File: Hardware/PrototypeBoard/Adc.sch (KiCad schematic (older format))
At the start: 30 parts, among them U5 ADC124S021

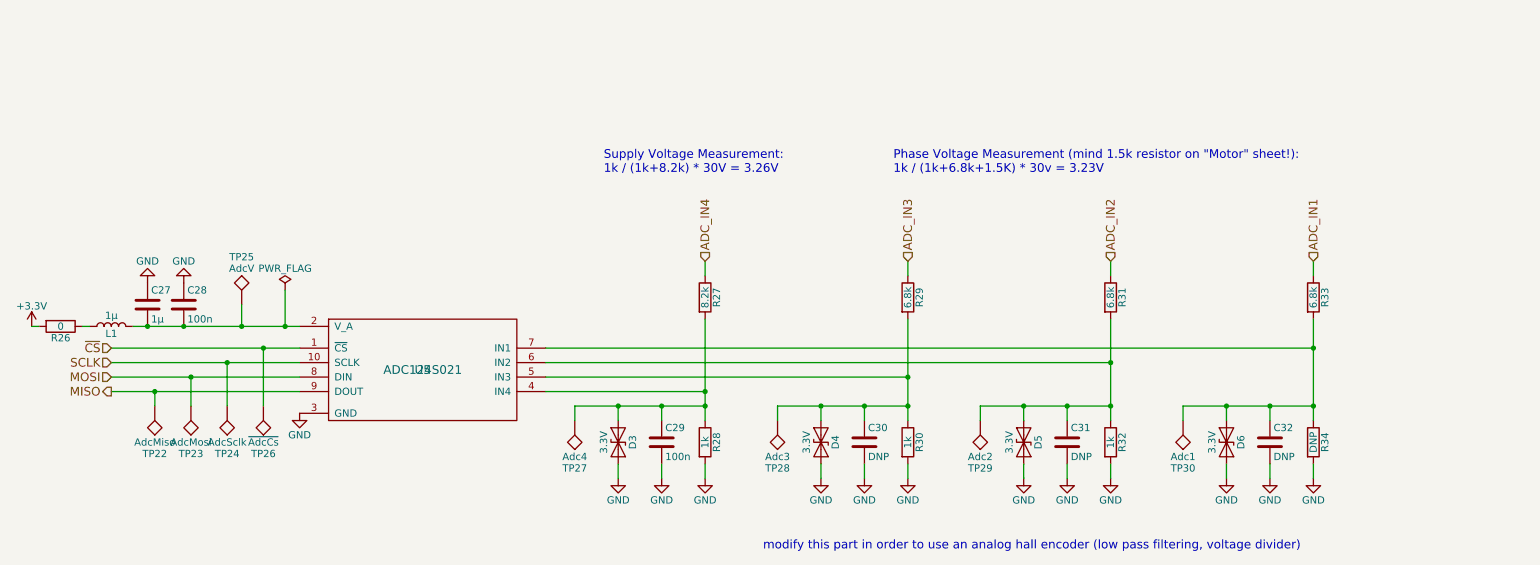
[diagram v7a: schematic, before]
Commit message: Added LEDs for PWM, SPI communication, Gate Driver Errors and Gate Driver disabled
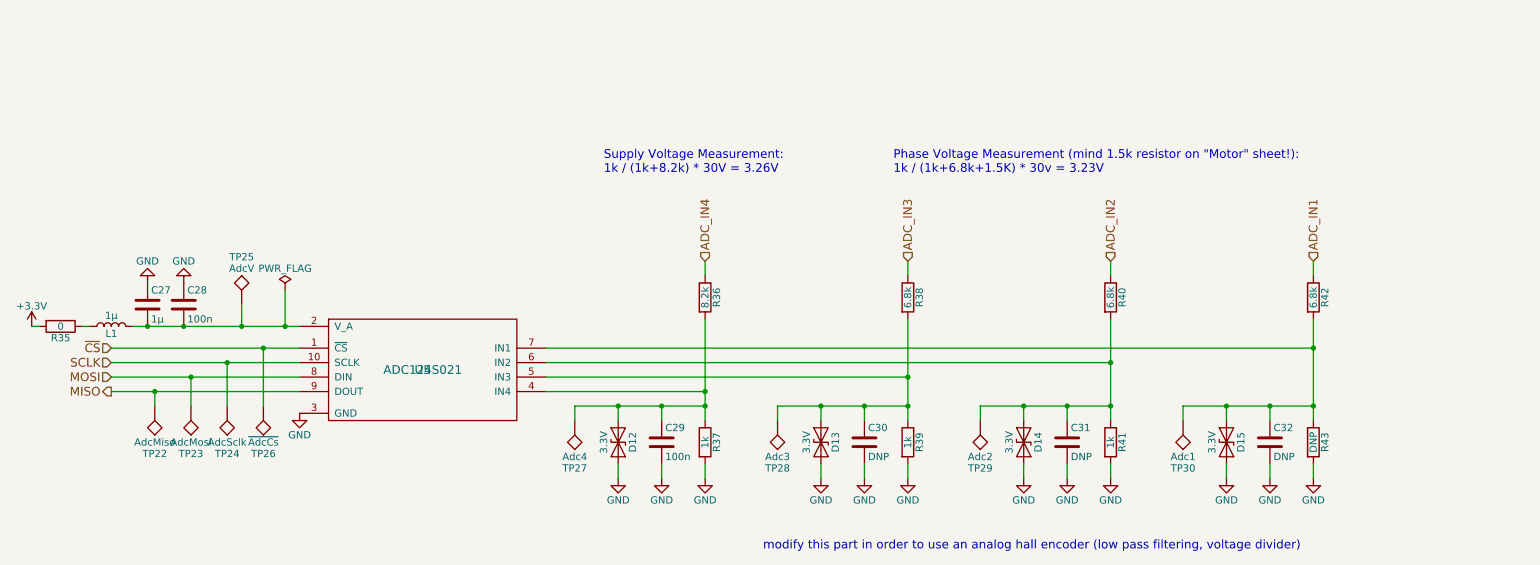
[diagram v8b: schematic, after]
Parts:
- renumbered D3 to D12, D4 to D13, D5 to D14, D6 to D15, R26 to R35, R27 to R36, R28 to R37, R29 to R38, R30 to R39, R31 to R40, R32 to R41, R33 to R42, R34 to R43
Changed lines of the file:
@@
 $EndComp
 $Comp
-L power:GND #PWR0104
+L power:GND #PWR058
 U 1 1 5AFC7F46
 P 2400 2950
-F 0 "#PWR0104" H 2400 2700 50  0001 C CNN
+F 0 "#PWR058" H 2400 2700 50  0001 C CNN
 F 1 "GND" H 2400 2800 50  0000 C CNN
 F 2 "" H 2400 2950 50  0001 C CNN
@@
 $EndComp
 $Comp
-L power:GND #PWR0105
+L power:GND #PWR057
 U 1 1 5AFC7FEF
 P 2150 2950
-F 0 "#PWR0105" H 2150 2700 50  0001 C CNN
+F 0 "#PWR057" H 2150 2700 50  0001 C CNN
 F 1 "GND" H 2150 2800 50  0000 C CNN
 F 2 "" H 2150 2950 50  0001 C CNN
@@
 $EndComp
 $Comp
-L power:+3.3V #PWR0106
+L power:+3.3V #PWR056
 U 1 1 5AFC801E
 P 1350 3250
-F 0 "#PWR0106" H 1350 3100 50  0001 C CNN
+F 0 "#PWR056" H 1350 3100 50  0001 C CNN
 F 1 "+3.3V" H 1350 3390 50  0000 C CNN
 F 2 "" H 1350 3250 50  0001 C CNN
@@
 Connection ~ 2400 3250
 $Comp
-L power:GND #PWR050
+L power:GND #PWR059
 U 1 1 5AFC8357
 P 3200 3850
-F 0 "#PWR050" H 3200 3600 50  0001 C CNN
+F 0 "#PWR059" H 3200 3600 50  0001 C CNN
 F 1 "GND" H 3200 3700 50  0000 C CNN
 F 2 "" H 3200 3850 50  0001 C CNN
@@
 $EndComp
 $Comp
-L Device:R R27
+L Device:R R36
 U 1 1 5AFD665A
 P 6000 3050
-F 0 "R27" V 6080 3050 50  0000 C CNN
+F 0 "R36" V 6080 3050 50  0000 C CNN
 F 1 "8.2k" V 6000 3050 50  0000 C CNN
 F 2 "Resistors_SMD:R_0805_HandSoldering" V 5930 3050 50  0001 C CNN
@@
 $EndComp
 $Comp
-L Device:R R29
+L Device:R R38
 U 1 1 5AFD6721
 P 7400 3050
-F 0 "R29" V 7480 3050 50  0000 C CNN
+F 0 "R38" V 7480 3050 50  0000 C CNN
 F 1 "6.8k" V 7400 3050 50  0000 C CNN
 F 2 "Resistors_SMD:R_0805_HandSoldering" V 7330 3050 50  0001 C CNN
@@
 $EndComp
 $Comp
-L Device:R R31
+L Device:R R40
 U 1 1 5AFD6757
 P 8800 3050
-F 0 "R31" V 8880 3050 50  0000 C CNN
+F 0 "R40" V 8880 3050 50  0000 C CNN
 F 1 "6.8k" V 8800 3050 50  0000 C CNN
 F 2 "Resistors_SMD:R_0805_HandSoldering" V 8730 3050 50  0001 C CNN
@@
 $EndComp
 $Comp
-L Device:R R33
+L Device:R R42
 U 1 1 5AFD6790
 P 10200 3050
-F 0 "R33" V 10280 3050 50  0000 C CNN
+F 0 "R42" V 10280 3050 50  0000 C CNN
 F 1 "6.8k" V 10200 3050 50  0000 C CNN
 F 2 "Resistors_SMD:R_0805_HandSoldering" V 10130 3050 50  0001 C CNN
@@
 	10200 2800 10200 2900
 $Comp
-L Device:R R34
+L Device:R R43
 U 1 1 5AFD684A
 P 10200 4050
-F 0 "R34" V 10280 4050 50  0000 C CNN
+F 0 "R43" V 10280 4050 50  0000 C CNN
 F 1 "DNP" V 10200 4050 50  0000 C CNN
 F 2 "Resistors_SMD:R_0805_HandSoldering" V 10130 4050 50  0001 C CNN
@@
 $EndComp
 $Comp
-L Device:R R32
+L Device:R R41
 U 1 1 5AFD68B5
 P 8800 4050
-F 0 "R32" V 8880 4050 50  0000 C CNN
+F 0 "R41" V 8880 4050 50  0000 C CNN
 F 1 "1k" V 8800 4050 50  0000 C CNN
 F 2 "Resistors_SMD:R_0805_HandSoldering" V 8730 4050 50  0001 C CNN
@@
 $EndComp
 $Comp
-L Device:R R30
+L Device:R R39
 U 1 1 5AFD6903
 P 7400 4050
-F 0 "R30" V 7480 4050 50  0000 C CNN
+F 0 "R39" V 7480 4050 50  0000 C CNN
 F 1 "1k" V 7400 4050 50  0000 C CNN
 F 2 "Resistors_SMD:R_0805_HandSoldering" V 7330 4050 50  0001 C CNN
@@
 $EndComp
 $Comp
-L Device:R R28
+L Device:R R37
 U 1 1 5AFD695A
 P 6000 4050
-F 0 "R28" V 6080 4050 50  0000 C CNN
+F 0 "R37" V 6080 4050 50  0000 C CNN
 F 1 "1k" V 6000 4050 50  0000 C CNN
 F 2 "Resistors_SMD:R_0805_HandSoldering" V 5930 4050 50  0001 C CNN
@@
 $EndComp
 $Comp
-L power:GND #PWR051
+L power:GND #PWR061
 U 1 1 5AFD6E2A
 P 5700 4300
-F 0 "#PWR051" H 5700 4050 50  0001 C CNN
+F 0 "#PWR061" H 5700 4050 50  0001 C CNN
 F 1 "GND" H 5700 4150 50  0000 C CNN
 F 2 "" H 5700 4300 50  0001 C CNN
@@
 $EndComp
 $Comp
-L power:GND #PWR052
+L power:GND #PWR062
 U 1 1 5AFD6E6C
 P 6000 4300
-F 0 "#PWR052" H 6000 4050 50  0001 C CNN
+F 0 "#PWR062" H 6000 4050 50  0001 C CNN
 F 1 "GND" H 6000 4150 50  0000 C CNN
 F 2 "" H 6000 4300 50  0001 C CNN
@@
 $EndComp
 $Comp
-L power:GND #PWR053
+L power:GND #PWR064
 U 1 1 5AFD6EA7
 P 7100 4300
-F 0 "#PWR053" H 7100 4050 50  0001 C CNN
+F 0 "#PWR064" H 7100 4050 50  0001 C CNN
 F 1 "GND" H 7100 4150 50  0000 C CNN
 F 2 "" H 7100 4300 50  0001 C CNN
@@
 $EndComp
 $Comp
-L power:GND #PWR054
+L power:GND #PWR065
 U 1 1 5AFD6EE2
 P 7400 4300
-F 0 "#PWR054" H 7400 4050 50  0001 C CNN
+F 0 "#PWR065" H 7400 4050 50  0001 C CNN
 F 1 "GND" H 7400 4150 50  0000 C CNN
 F 2 "" H 7400 4300 50  0001 C CNN
@@
 $EndComp
 $Comp
-L power:GND #PWR055
+L power:GND #PWR067
 U 1 1 5AFD6F1D
 P 8500 4300
-F 0 "#PWR055" H 8500 4050 50  0001 C CNN
+F 0 "#PWR067" H 8500 4050 50  0001 C CNN
 F 1 "GND" H 8500 4150 50  0000 C CNN
 F 2 "" H 8500 4300 50  0001 C CNN
@@
 $EndComp
 $Comp
-L power:GND #PWR056
+L power:GND #PWR068
 U 1 1 5AFD6F58
 P 8800 4300
-F 0 "#PWR056" H 8800 4050 50  0001 C CNN
+F 0 "#PWR068" H 8800 4050 50  0001 C CNN
 F 1 "GND" H 8800 4150 50  0000 C CNN
 F 2 "" H 8800 4300 50  0001 C CNN
@@
 $EndComp
 $Comp
-L power:GND #PWR057
+L power:GND #PWR070
 U 1 1 5AFD6F93
 P 9900 4300
-F 0 "#PWR057" H 9900 4050 50  0001 C CNN
+F 0 "#PWR070" H 9900 4050 50  0001 C CNN
 F 1 "GND" H 9900 4150 50  0000 C CNN
 F 2 "" H 9900 4300 50  0001 C CNN
@@
 $EndComp
 $Comp
-L power:GND #PWR058
+L power:GND #PWR071
 U 1 1 5AFD6FCE
 P 10200 4300
-F 0 "#PWR058" H 10200 4050 50  0001 C CNN
+F 0 "#PWR071" H 10200 4050 50  0001 C CNN
 F 1 "GND" H 10200 4150 50  0000 C CNN
 F 2 "" H 10200 4300 50  0001 C CNN
@@
 Connection ~ 2950 3400
 $Comp
-L power:PWR_FLAG #FLG059
+L power:PWR_FLAG #FLG02
 U 1 1 5AFF7DCE
 P 3100 3000
-F 0 "#FLG059" H 3100 3075 50  0001 C CNN
+F 0 "#FLG02" H 3100 3075 50  0001 C CNN
 F 1 "PWR_FLAG" H 3100 3150 50  0000 C CNN
 F 2 "" H 3100 3000 50  0001 C CNN
@@
 $EndComp
 $Comp
-L power:GND #PWR061
+L power:GND #PWR063
 U 1 1 5B002BCE
 P 6800 4300
-F 0 "#PWR061" H 6800 4050 50  0001 C CNN
+F 0 "#PWR063" H 6800 4050 50  0001 C CNN
 F 1 "GND" H 6800 4150 50  0000 C CNN
 F 2 "" H 6800 4300 50  0001 C CNN
@@
 $EndComp
 $Comp
-L power:GND #PWR062
+L power:GND #PWR066
 U 1 1 5B002C30
 P 8200 4300
-F 0 "#PWR062" H 8200 4050 50  0001 C CNN
+F 0 "#PWR066" H 8200 4050 50  0001 C CNN
 F 1 "GND" H 8200 4150 50  0000 C CNN
 F 2 "" H 8200 4300 50  0001 C CNN
@@
 $EndComp
 $Comp
-L power:GND #PWR063
+L power:GND #PWR069
 U 1 1 5B002C92
 P 9600 4300
-F 0 "#PWR063" H 9600 4050 50  0001 C CNN
+F 0 "#PWR069" H 9600 4050 50  0001 C CNN
 F 1 "GND" H 9600 4150 50  0000 C CNN
 F 2 "" H 9600 4300 50  0001 C CNN
@@
 modify this part in order to use an analog hall encoder (low pass filtering, voltage divider)
 $Comp
-L Device:D_TVS D6
+L Device:D_TVS D15
 U 1 1 5AFF1E54
 P 9600 4050
-F 0 "D6" H 9600 4150 50  0000 C CNN
+F 0 "D15" H 9600 4150 50  0000 C CNN
 F 1 "3.3V" H 9600 3950 50  0000 C CNN
 F 2 "Diodes_SMD:D_SOD-323_HandSoldering" H 9600 4050 50  0001 C CNN
@@
 $EndComp
 $Comp
-L Device:D_TVS D3
+L Device:D_TVS D12
 U 1 1 5AFF1F87
 P 5400 4050
-F 0 "D3" H 5400 4150 50  0000 C CNN
+F 0 "D12" H 5400 4150 50  0000 C CNN
 F 1 "3.3V" H 5400 3950 50  0000 C CNN
 F 2 "Diodes_SMD:D_SOD-323_HandSoldering" H 5400 4050 50  0001 C CNN
@@
 $EndComp
 $Comp
-L Device:D_TVS D4
+L Device:D_TVS D13
 U 1 1 5AFF2000
 P 6800 4050
-F 0 "D4" H 6800 4150 50  0000 C CNN
+F 0 "D13" H 6800 4150 50  0000 C CNN
 F 1 "3.3V" H 6800 3950 50  0000 C CNN
 F 2 "Diodes_SMD:D_SOD-323_HandSoldering" H 6800 4050 50  0001 C CNN
@@
 $EndComp
 $Comp
-L Device:D_TVS D5
+L Device:D_TVS D14
 U 1 1 5AFF208E
 P 8200 4050
-F 0 "D5" H 8200 4150 50  0000 C CNN
+F 0 "D14" H 8200 4150 50  0000 C CNN
 F 1 "3.3V" H 8200 3950 50  0000 C CNN
 F 2 "Diodes_SMD:D_SOD-323_HandSoldering" H 8200 4050 50  0001 C CNN
@@
 $EndComp
 $Comp
-L Device:R R26
+L Device:R R35
 U 1 1 5B210B75
 P 1550 3250
-F 0 "R26" V 1630 3250 50  0000 C CNN
+F 0 "R35" V 1630 3250 50  0000 C CNN
 F 1 "0" V 1550 3250 50  0000 C CNN
 F 2 "Resistors_SMD:R_0805_HandSoldering" V 1480 3250 50  0001 C CNN
